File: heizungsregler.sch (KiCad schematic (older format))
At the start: 15 parts, among them J101 RPi_GPIO, J102 Conn_01x03_Male, J103 Conn_01x10_Male, U101 oled_0.96\", U102 DS18B20

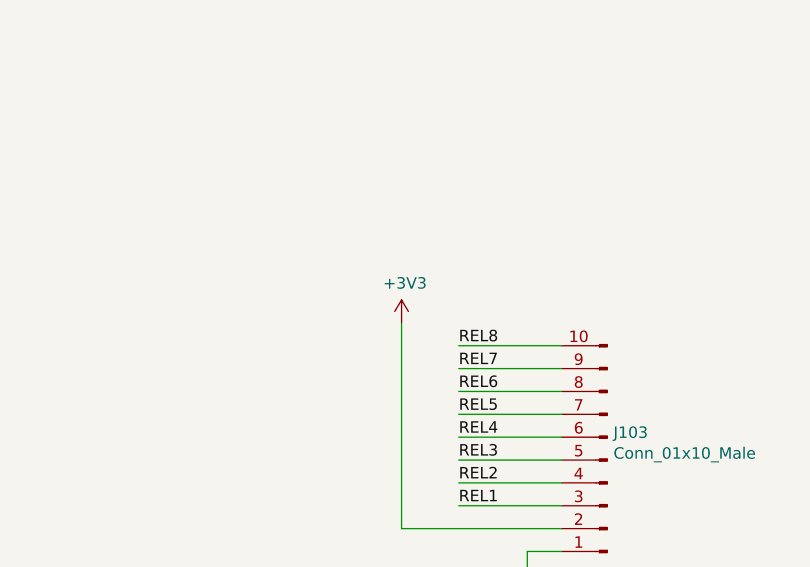
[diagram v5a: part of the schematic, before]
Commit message: Relais geroutet
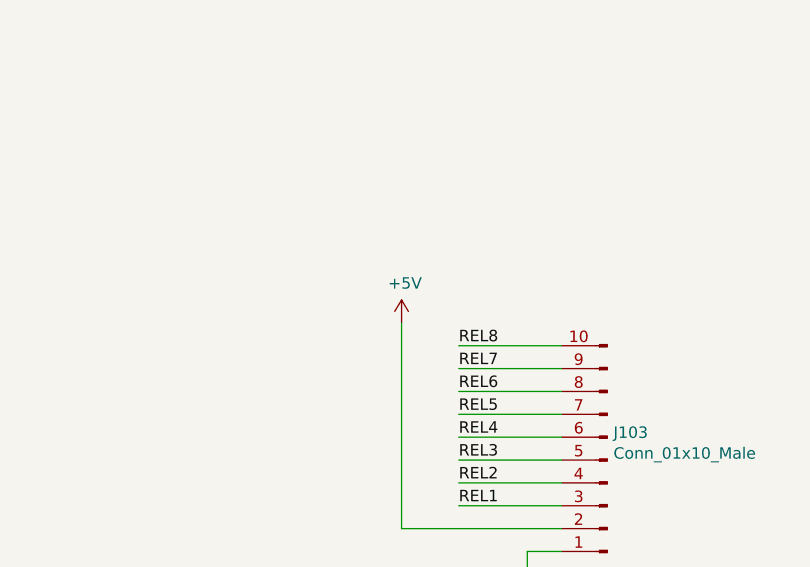
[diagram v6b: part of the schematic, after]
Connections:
- net +3V3: no longer J103.2 (Pin_2)
- net +5V: now also J103.2 (Pin_2)
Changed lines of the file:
@@
 Wire Wire Line
 	5800 7150 5800 7250
-$Comp
-L power:+3V3 #PWR0108
-U 1 1 5C11E858
-P 5250 6150
-F 0 "#PWR0108" H 5250 6000 50  0001 C CNN
-F 1 "+3V3" H 5265 6323 50  0000 C CNN
-F 2 "" H 5250 6150 50  0001 C CNN
-F 3 "" H 5250 6150 50  0001 C CNN
-	1    5250 6150
-	1    0    0    -1
-$EndComp
 Text Label 5500 6950 0    50   ~ 0
 REL1
@@
 Wire Wire Line
 	8950 3650 8950 3900
+$Comp
+L power:+5V #PWR?
+U 1 1 5C0C787A
+P 5250 6150
+F 0 "#PWR?" H 5250 6000 50  0001 C CNN
+F 1 "+5V" H 5265 6323 50  0000 C CNN
+F 2 "" H 5250 6150 50  0001 C CNN
+F 3 "" H 5250 6150 50  0001 C CNN
+	1    5250 6150
+	1    0    0    -1
+$EndComp
 $EndSCHEMATC

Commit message: Transistoren für Relais eingefügt, Pull-Ups für I2C, zusätzlicher Spannungseingang, Layout fertig
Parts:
- removed J103: Conn_01x10_Male, Connector_PinHeader_2.54mm:PinHeader_1x10_P2.54mm_Vertical, symbol Connector:Conn_01x10_Male
- added J103: Conn_01x02, Connector_Phoenix_MSTB:PhoenixContact_MSTBVA_2,5_2-G-5,08_1x02_P5.08mm_Vertical, symbol Connector_Generic:Conn_01x02
- added J104: Conn_01x03_Male, Connector_PinHeader_2.54mm:PinHeader_1x03_P2.54mm_Vertical, symbol Connector:Conn_01x03_Male
- added J105: Conn_01x04_Male, Connector_PinHeader_2.54mm:PinHeader_1x04_P2.54mm_Vertical, symbol Connector:Conn_01x04_Male
- added R102, R103: 0R00, Resistor_SMD:R_1206_3216Metric, symbol Device:R
- added R104: R, Resistor_SMD:R_0603_1608Metric, symbol Device:R
- added R105, R106: 2K2, Resistor_SMD:R_1206_3216Metric, symbol Device:R
- H105, H106, H107, H108: symbol Mechanical:MountingHole -> Mechanical:MountingHole_Pad
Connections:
- net +3V3: now also J105.2 (Pin_2), R104.1, R105.1, R106.1; no longer C101.1, J101.17 (3.3V), J102.2 (Pin_2), U102.3 (VDD)
- net +5V: now also R102.1
- net DQ: now also J104.3 (Pin_3)
- net GND: now also H105.1, H106.1, H107.1, H108.1, J103.1 (Pin_1), J104.1 (Pin_1), J105.1 (Pin_1)
- net SCL: now also J105.3 (Pin_3), R106.2
- net SDA: now also J105.4 (Pin_4), R105.2
- new net: C101.1, J102.2 (Pin_2), J104.2 (Pin_2), R104.2, U102.3 (VDD)
- new net: J103.2 (Pin_2), R102.2, R103.2
- new net +24V: R103.1
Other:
- moved on the sheet: C101, J102, R101, U102
